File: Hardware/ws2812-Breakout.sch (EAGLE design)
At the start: 10 parts, among them U1 LED-TRICOLOR-5050

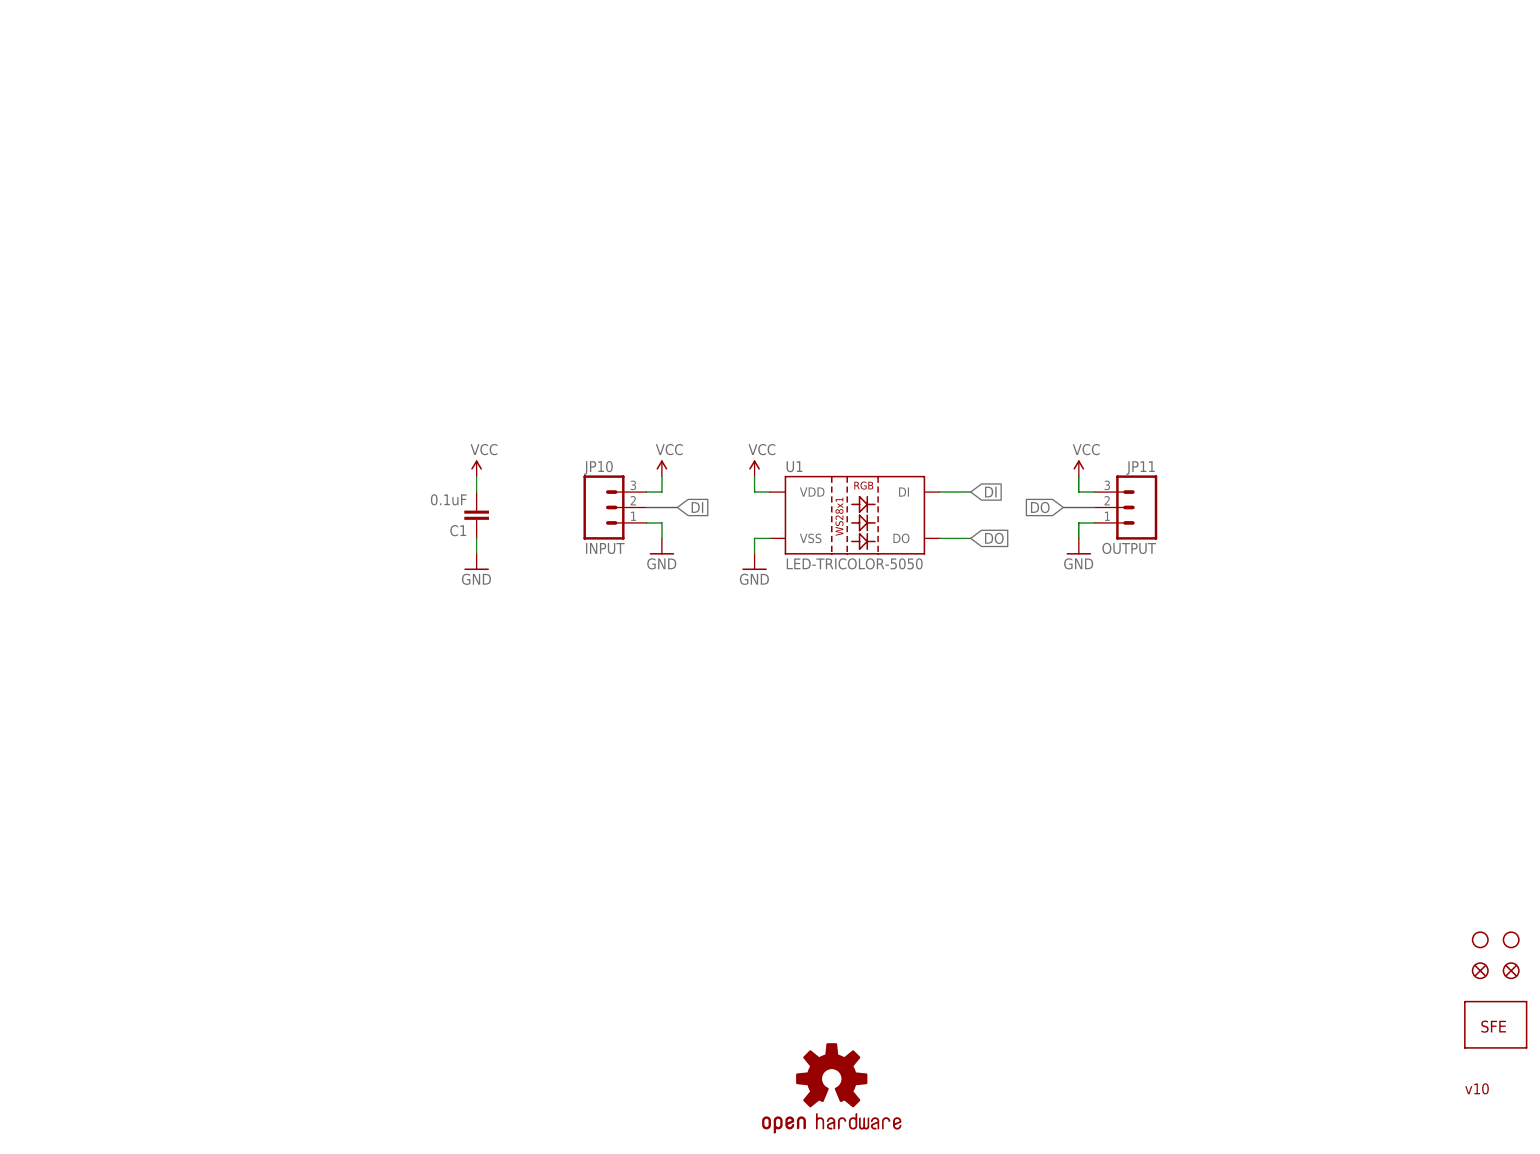
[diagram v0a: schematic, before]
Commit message: Updating repo structure, adding firmware, README and .gitignore
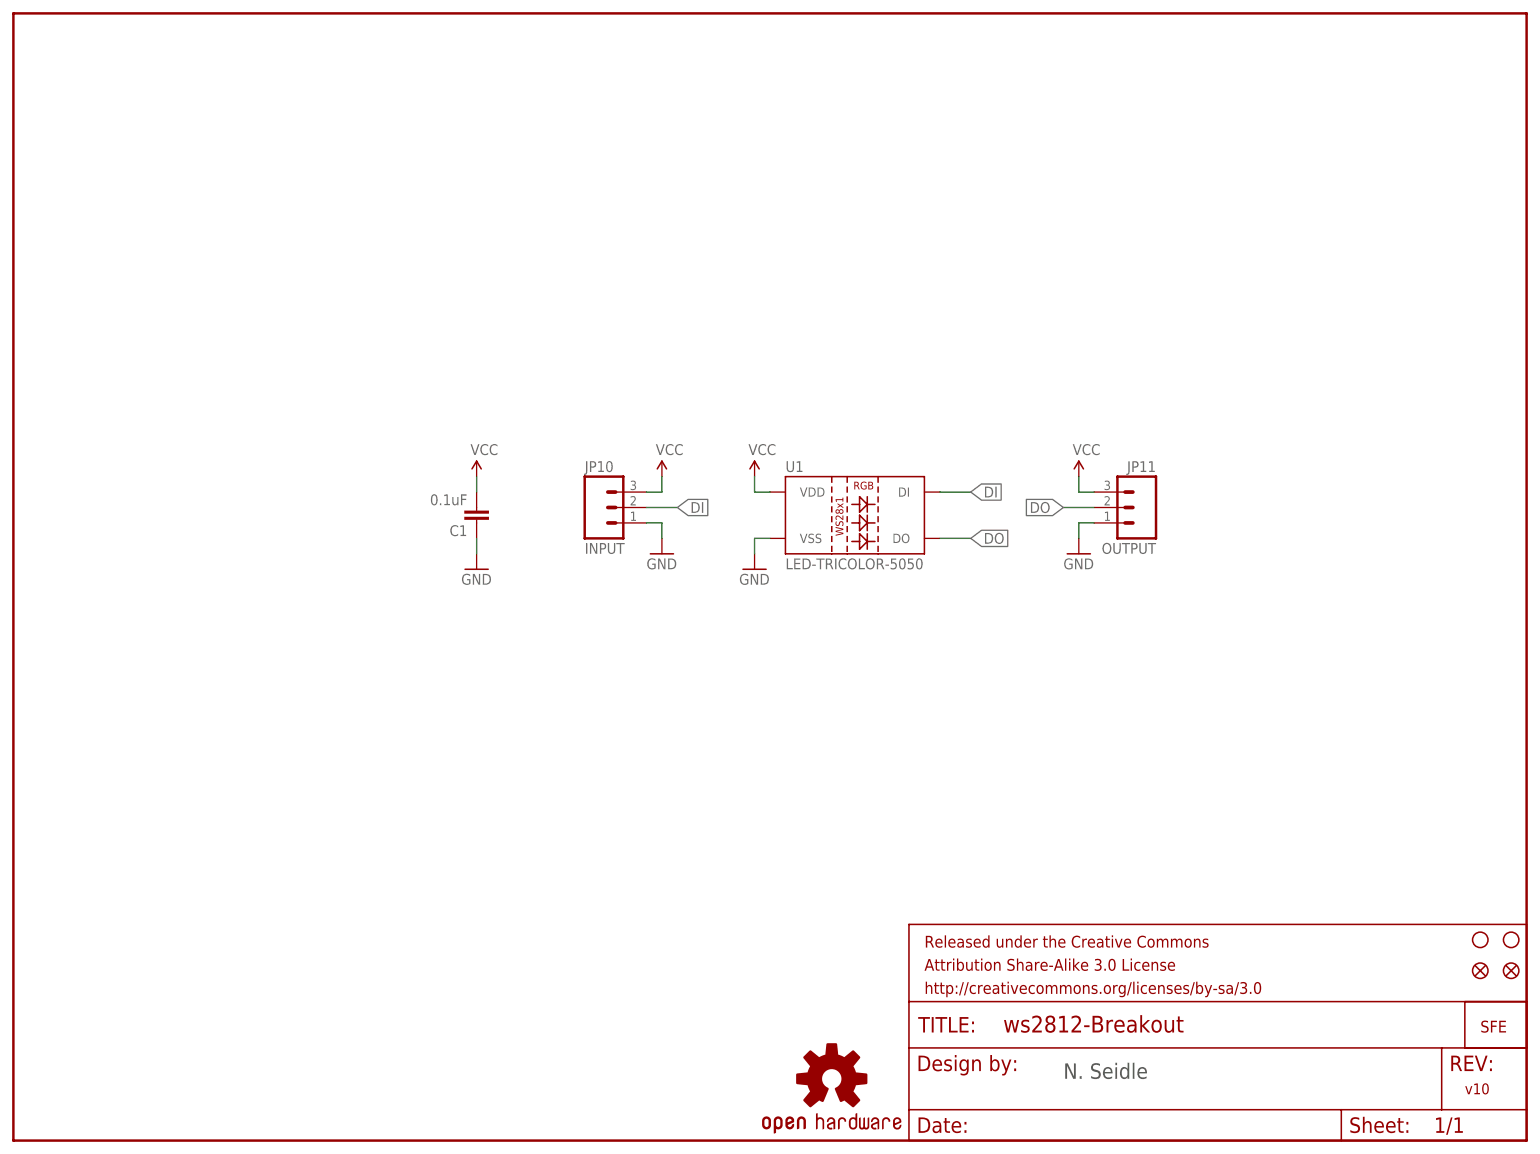
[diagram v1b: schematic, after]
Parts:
- added FRAME1: FRAME-LETTER, SparkFun-Aesthetics:FRAME-LETTER
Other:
- note added: "N. Seidle"
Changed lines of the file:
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@@
 </classes>
 <parts>
-<part name="FRAME1" library="SparkFun" deviceset="FRAME-LETTER" device=""/>
+<part name="FRAME1" library="SparkFun-Aesthetics" deviceset="FRAME-LETTER" device=""/>
 <part name="P+1" library="SparkFun" deviceset="VCC" device=""/>
 <part name="GND1" library="SparkFun" deviceset="GND" device=""/>
@@
 <plain>
 <text x="238.76" y="7.62" size="1.778" layer="94">v10</text>
+<text x="172.72" y="10.16" size="2.54" layer="97">N. Seidle</text>
 </plain>
 <instances>
